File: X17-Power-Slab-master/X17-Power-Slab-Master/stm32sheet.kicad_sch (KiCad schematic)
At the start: 15 parts, among them J1 Conn_01x05, U4 STM32F091CCTx, Y2 8MHz

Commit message: Schematic Updates
#SlayedTheDayAway
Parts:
- removed J1: Conn_01x05, symbol Connector_Generic:Conn_01x05
- added C18: 0.1uF, symbol Device:C
- added J1: 61201021621, 612_STMconn:61201021621, symbol STM32_Connector:6120XX21621_61201021621
- added R26: 10k, symbol Device:R_US
- added SW1: SW_SPST, symbol Switch:SW_SPST
- added U7: ABLS-8.000MHZ-B2-T, footprints:ABLS-8.000MHZ-B2-T_ABR, symbol STM32_Oscillator:ABLS-8.000MHZ-B2-T
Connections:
- net NRST is gone; now on net GND: U4.7 (NRST)
- net 3.3V: now also J1.7, R26.1
- net GND: now also C18.2, J1.1, J1.3, J1.4, SW1.2 (B)
- net SWCLK: now also J1.6
- net SWDIO: now also J1.2
- new net: C18.1, R26.2, SW1.1 (A)
- new net 3.3: U7.2
- new net 5V: J1.9, U7.1
- no-connect marks 17 -> 24
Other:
- note added: "External Oscillator for STM32F0 8MHz ECS-2520MV-080-CN-TR"

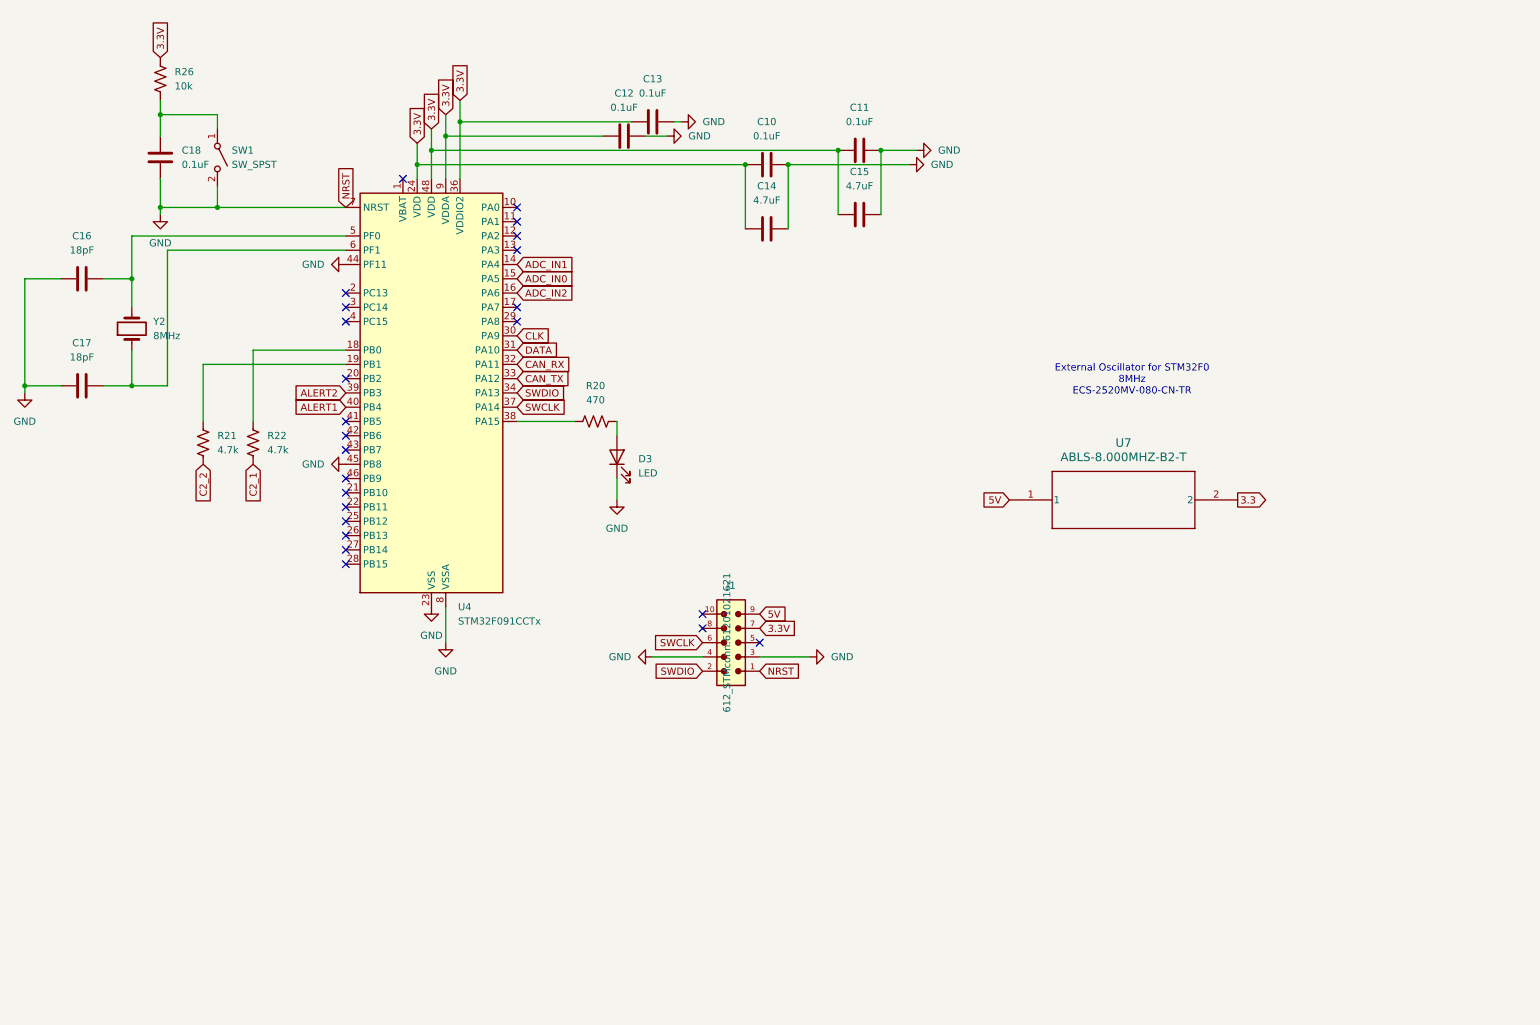
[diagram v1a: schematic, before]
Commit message: Schematic Full Update
Probs can start pacing after this.
Diode on RVP changed,
Button changed
Reverse voltage updated
Symbols updated to remove DRCs
GNDs changed
Connector updated
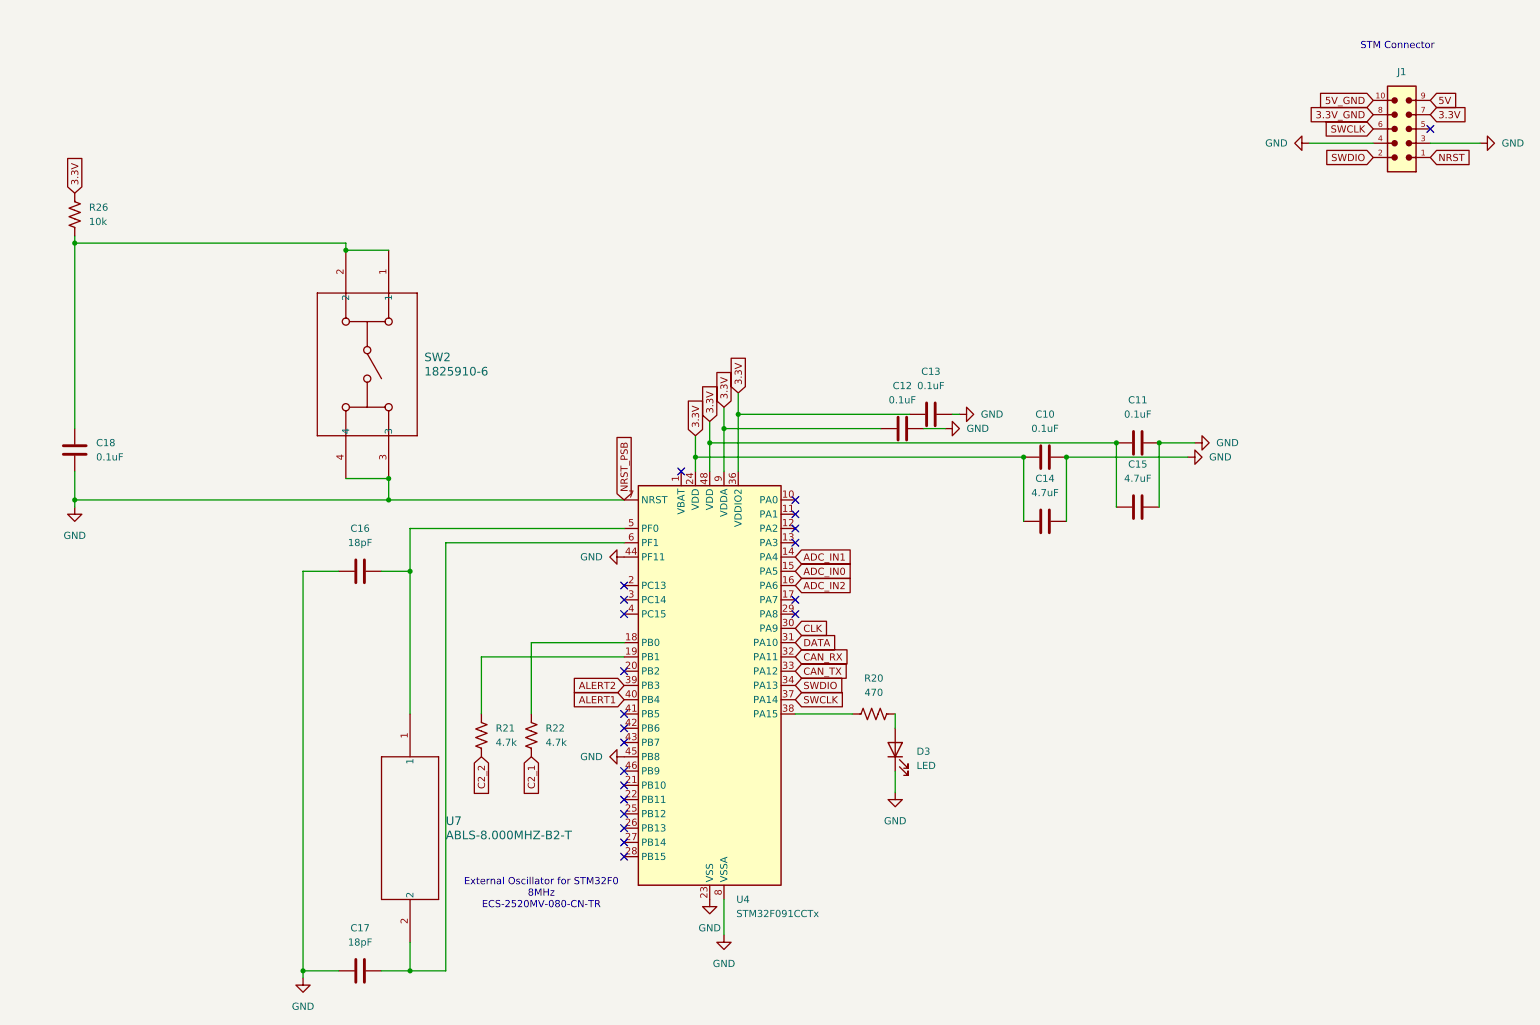
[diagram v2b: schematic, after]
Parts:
- removed SW1: SW_SPST, symbol Switch:SW_SPST
- removed Y2: 8MHz, symbol Device:Crystal
- added SW2: 1825910-6, SW4_1825910-B_TEC, symbol STM Switch Symbol:1825910-6
- C10, C11, C12, C13, C14, C15, C16, C17, C18: footprint (none) -> Capacitor_SMD:C_0603_1608Metric_Pad1.08x0.95mm_HandSolder
- D3: footprint (none) -> LED_SMD:LED_0805_2012Metric_Pad1.15x1.40mm_HandSolder
- J1: footprint 612_STMconn:61201021621 -> 6120XX21621_61201021621:61201021621
- R20, R21, R22, R26: footprint (none) -> Resistor_SMD:R_0603_1608Metric_Pad0.98x0.95mm_HandSolder
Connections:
- net 3.3 is gone; now on an unnamed net: U7.2
- net 5V: no longer U7.1
- net GND: now also SW2.3, SW2.4; no longer J1.1
- net at C18.1, R26.2: now also SW2.1, SW2.2
- net at C16.1, U4.5 (PF0): now also U7.1
- net 5V_GND: now reaches J1.10
- net 3.3V_GND: now reaches J1.8
- new net NRST: J1.1
- no-connect marks 24 -> 22
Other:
- note added: "STM Connector"
- moved on the sheet: C10, C11, C12, C13, C14, C15, C16, C17, C18, D3, R20, R21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

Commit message: Initial Placements
Issue - NRST_PSB is apparently ground flag
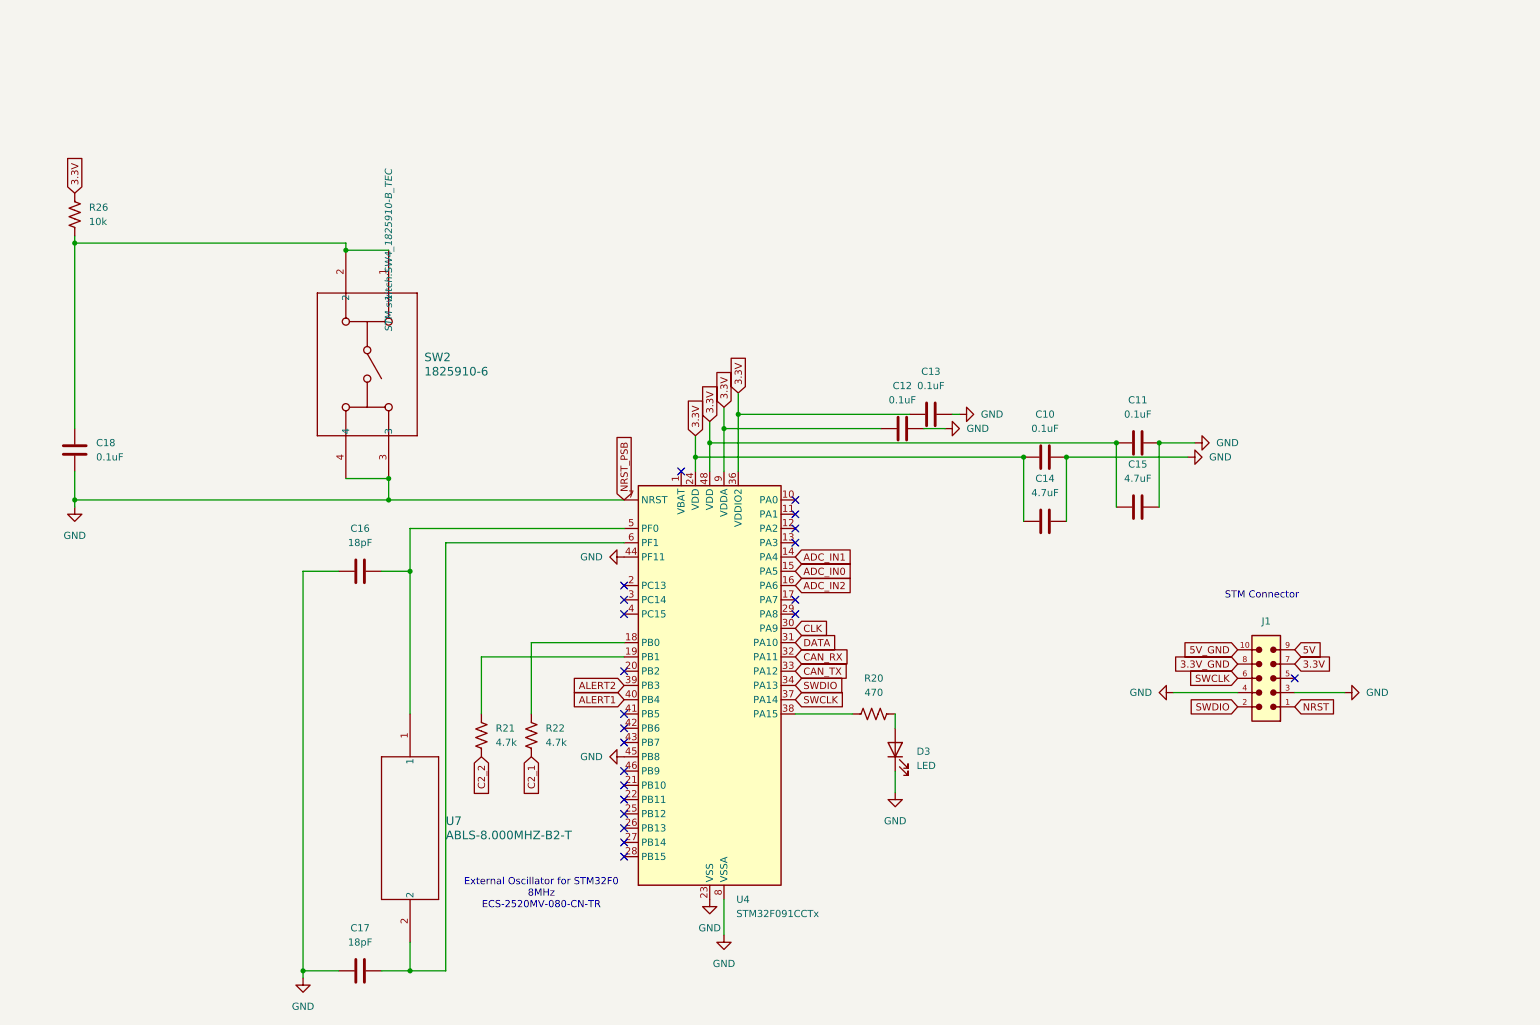
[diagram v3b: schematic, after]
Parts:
- J1: footprint 6120XX21621_61201021621:61201021621 -> 612_STMconn:61201021621
- SW2: footprint SW4_1825910-B_TEC -> STM switch:SW4_1825910-B_TEC
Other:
- moved on the sheet: J1
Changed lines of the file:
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@@
 	)
 	(no_connect
-		(at 266.7 36.83)
+		(at 242.57 134.62)
 	)
 	(no_connect
@@
 	(wire
 		(pts
-			(xy 266.7 39.37) (xy 275.59 39.37)
+			(xy 242.57 137.16) (xy 251.46 137.16)
 		)
 		(stroke
@@
 	(wire
 		(pts
-			(xy 245.11 39.37) (xy 256.54 39.37)
+			(xy 220.98 137.16) (xy 232.41 137.16)
 		)
 		(stroke
@@
 	(text "STM Connector\n"
 		(exclude_from_sim no)
-		(at 260.858 22.098 0)
+		(at 236.728 119.888 0)
 		(effects
 			(font
@@
 	(global_label "SWCLK"
 		(shape input)
-		(at 256.54 36.83 180)
+		(at 232.41 134.62 180)
 		(fields_autoplaced yes)
 		(effects
@@
 		)
 		(property "Intersheetrefs" "${INTERSHEET_REFS}"
-			(at 247.3258 36.83 0)
+			(at 223.1958 134.62 0)
 			(effects
 				(font
@@
 	(global_label "5V_GND"
 		(shape input)
-		(at 256.54 31.75 180)
+		(at 232.41 129.54 180)
 		(fields_autoplaced yes)
 		(effects
@@
 		)
 		(property "Intersheetrefs" "${INTERSHEET_REFS}"
-			(at 246.4186 31.75 0)
+			(at 222.2886 129.54 0)
 			(effects
 				(font
@@
 	(global_label "3.3V_GND"
 		(shape input)
-		(at 256.54 34.29 180)
+		(at 232.41 132.08 180)
 		(fields_autoplaced yes)
 		(effects
@@
 		)
 		(property "Intersheetrefs" "${INTERSHEET_REFS}"
-			(at 244.6043 34.29 0)
+			(at 220.4743 132.08 0)
 			(effects
 				(font
@@
 	(global_label "NRST"
 		(shape input)
-		(at 266.7 41.91 0)
+		(at 242.57 139.7 0)
 		(fields_autoplaced yes)
 		(effects
@@
 		)
 		(property "Intersheetrefs" "${INTERSHEET_REFS}"
-			(at 274.4628 41.91 0)
+			(at 250.3328 139.7 0)
 			(effects
 				(font
@@
 	(global_label "5V"
 		(shape input)
-		(at 266.7 31.75 0)
+		(at 242.57 129.54 0)
 		(fields_autoplaced yes)
 		(effects
@@
 		)
 		(property "Intersheetrefs" "${INTERSHEET_REFS}"
-			(at 271.9833 31.75 0)
+			(at 247.8533 129.54 0)
 			(effects
 				(font
@@
 	(global_label "SWDIO"
 		(shape input)
-		(at 256.54 41.91 180)
+		(at 232.41 139.7 180)
 		(fields_autoplaced yes)
 		(effects
@@
 		)
 		(property "Intersheetrefs" "${INTERSHEET_REFS}"
-			(at 247.6886 41.91 0)
+			(at 223.5586 139.7 0)
 			(effects
 				(font
@@
 	(global_label "3.3V"
 		(shape input)
-		(at 266.7 34.29 0)
+		(at 242.57 132.08 0)
 		(fields_autoplaced yes)
 		(effects
@@
 		)
 		(property "Intersheetrefs" "${INTERSHEET_REFS}"
-			(at 273.7976 34.29 0)
+			(at 249.6676 132.08 0)
 			(effects
 				(font
@@
 			)
 		)
-		(property "Footprint" "SW4_1825910-B_TEC"
+		(property "Footprint" "STM switch:SW4_1825910-B_TEC"
 			(at 81.28 58.42 0)
 			(effects
@@
 					(italic yes)
 				)
-				(hide yes)
 			)
 		)
@@
 	(symbol
 		(lib_id "power:GND")
-		(at 245.11 39.37 270)
+		(at 220.98 137.16 270)
 		(unit 1)
 		(exclude_from_sim no)
@@
 		(fields_autoplaced yes)
 		(property "Reference" "#PWR08"
-			(at 238.76 39.37 0)
+			(at 214.63 137.16 0)
 			(effects
 				(font
@@
 		)
 		(property "Value" "GND"
-			(at 241.3 39.3699 90)
+			(at 217.17 137.1599 90)
 			(effects
 				(font
@@
 		)
 		(property "Footprint" ""
-			(at 245.11 39.37 0)
+			(at 220.98 137.16 0)
 			(effects
 				(font
@@
 		)
 		(property "Datasheet" ""
-			(at 245.11 39.37 0)
+			(at 220.98 137.16 0)
 			(effects
 				(font
@@
 		)
 		(property "Description" "Power symbol creates a global label with name \"GND\" , ground"
-			(at 245.11 39.37 0)
+			(at 220.98 137.16 0)
 			(effects
 				(font
@@
 	(symbol
 		(lib_id "STM32_Connector:6120XX21621_61201021621")
-		(at 261.62 36.83 90)
+		(at 237.49 134.62 90)
 		(unit 1)
 		(exclude_from_sim no)
@@
 		(fields_autoplaced yes)
 		(property "Reference" "J1"
-			(at 261.62 26.67 90)
+			(at 237.49 124.46 90)
 			(effects
 				(font
@@
 		)
 		(property "Value" "61201021621"
-			(at 261.62 36.83 0)
+			(at 237.49 134.62 0)
 			(effects
 				(font
@@
 			)
 		)
-		(property "Footprint" "6120XX21621_61201021621:61201021621"
-			(at 261.62 36.83 0)
+		(property "Footprint" "612_STMconn:61201021621"
+			(at 237.49 134.62 0)
 			(effects
 				(font
@@
 		)
 		(property "Datasheet" ""
-			(at 261.62 36.83 0)
+			(at 237.49 134.62 0)
 			(effects
 				(font
@@
 		)
 		(property "Description" ""
-			(at 261.62 36.83 0)
+			(at 237.49 134.62 0)
 			(effects
 				(font
@@
 		)
 		(property "CONTACT-RESISTANCE" "20mOhm"
-			(at 261.62 36.83 0)
+			(at 237.49 134.62 0)
 			(effects
 				(font
@@
 		)
 		(property "GENDER" "Male"
-			(at 261.62 36.83 0)
+			(at 237.49 134.62 0)
 			(effects
 				(font
@@
 		)
 		(property "MOUNT" "THT"
-			(at 261.62 36.83 0)
+			(at 237.49 134.62 0)
 			(effects
 				(font
@@
 		)
 		(property "IR" "3A"
-			(at 261.62 36.83 0)
+			(at 237.49 134.62 0)
 			(effects
 				(font
@@
 		)
 		(property "PACKAGING" "Tray"
-			(at 261.62 36.83 0)
+			(at 237.49 134.62 0)
 			(effects
 				(font
@@
 		)
 		(property "PART-NUMBER" "61201021621"
-			(at 261.62 36.83 0)
+			(at 237.49 134.62 0)
 			(effects
 				(font
@@
 		)
 		(property "LENGTH" "20.36mm"
-			(at 261.62 36.83 0)
+			(at 237.49 134.62 0)
 			(effects
 				(font
@@
 		)
 		(property "DATASHEET-URL" "https://www.we-online.com/redexpert/spec/61201021621?ae"
-			(at 261.62 36.83 0)
+			(at 237.49 134.62 0)
 			(effects
 				(font
@@
 		)
 		(property "WORKING-VOLTAGE" "250V(AC)"
-			(at 261.62 36.83 0)
+			(at 237.49 134.62 0)
 			(effects
 				(font
@@
 		)
 		(property "PINS" "10"
-			(at 261.62 36.83 0)
+			(at 237.49 134.62 0)
 			(effects
 				(font
@@
 		)
 		(property "PITCH" "2.54mm"
-			(at 261.62 36.83 0)
+			(at 237.49 134.62 0)
 			(effects
 				(font
@@
 		)
 		(property "TYPE" "Straight"
-			(at 261.62 36.83 0)
+			(at 237.49 134.62 0)
 			(effects
 				(font
@@
 	(symbol
 		(lib_id "power:GND")
-		(at 275.59 39.37 90)
+		(at 251.46 137.16 90)
 		(unit 1)
 		(exclude_from_sim no)
@@
 		(fields_autoplaced yes)
 		(property "Reference" "#PWR04"
-			(at 281.94 39.37 0)
+			(at 257.81 137.16 0)
 			(effects
 				(font
@@
 		)
 		(property "Value" "GND"
-			(at 279.4 39.3699 90)
+			(at 255.27 137.1599 90)
 			(effects
 				(font
@@
 		)
 		(property "Footprint" ""
-			(at 275.59 39.37 0)
+			(at 251.46 137.16 0)
 			(effects
 				(font
@@
 		)
 		(property "Datasheet" ""
-			(at 275.59 39.37 0)
+			(at 251.46 137.16 0)
 			(effects
 				(font
@@
 		)
 		(property "Description" "Power symbol creates a global label with name \"GND\" , ground"
-			(at 275.59 39.37 0)
+			(at 251.46 137.16 0)
 			(effects
 				(font
